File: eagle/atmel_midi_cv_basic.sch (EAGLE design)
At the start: 46 parts, among them IC1 TL074P, Q2 2N3904, U1 ATMEGA328P_PDIP

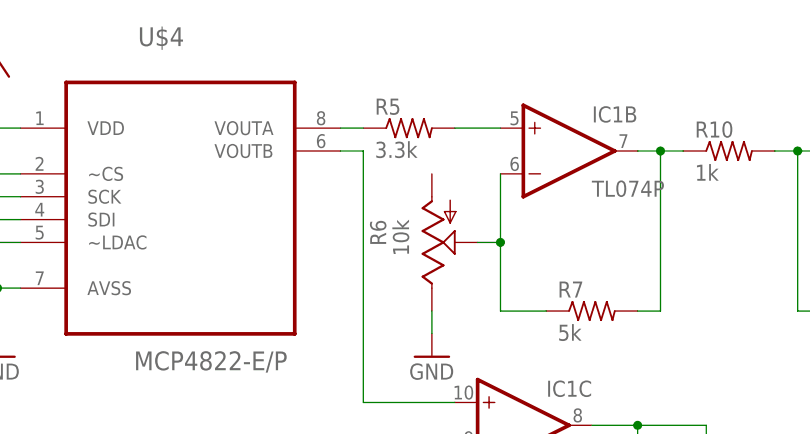
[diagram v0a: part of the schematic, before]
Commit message: playing scale to indicate midi channel by number of notes
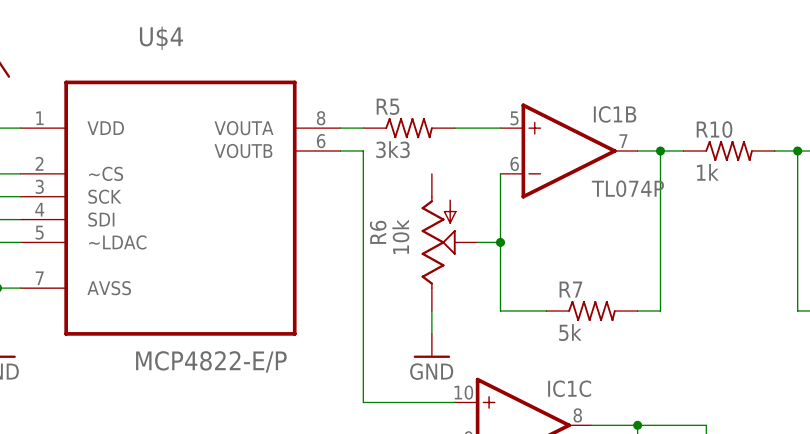
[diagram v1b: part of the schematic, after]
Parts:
- R5: value 3.3k -> 3k3
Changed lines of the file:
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@@
 <?xml version="1.0" encoding="utf-8"?>
 <!DOCTYPE eagle SYSTEM "eagle.dtd">
-<eagle version="7.2.0">
+<eagle version="7.1.0">
 <drawing>
 <settings>
@@
 <part name="GND1" library="supply1" deviceset="GND" device=""/>
 <part name="GND2" library="supply1" deviceset="GND" device=""/>
-<part name="R5" library="rcl" deviceset="R-US_" device="0207/10" value="3.3k"/>
+<part name="R5" library="rcl" deviceset="R-US_" device="0207/10" value="3k3"/>
 <part name="R6" library="pot" deviceset="TRIM_US-" device="B64W" value="10k"/>
 <part name="GND4" library="supply1" deviceset="GND" device=""/>

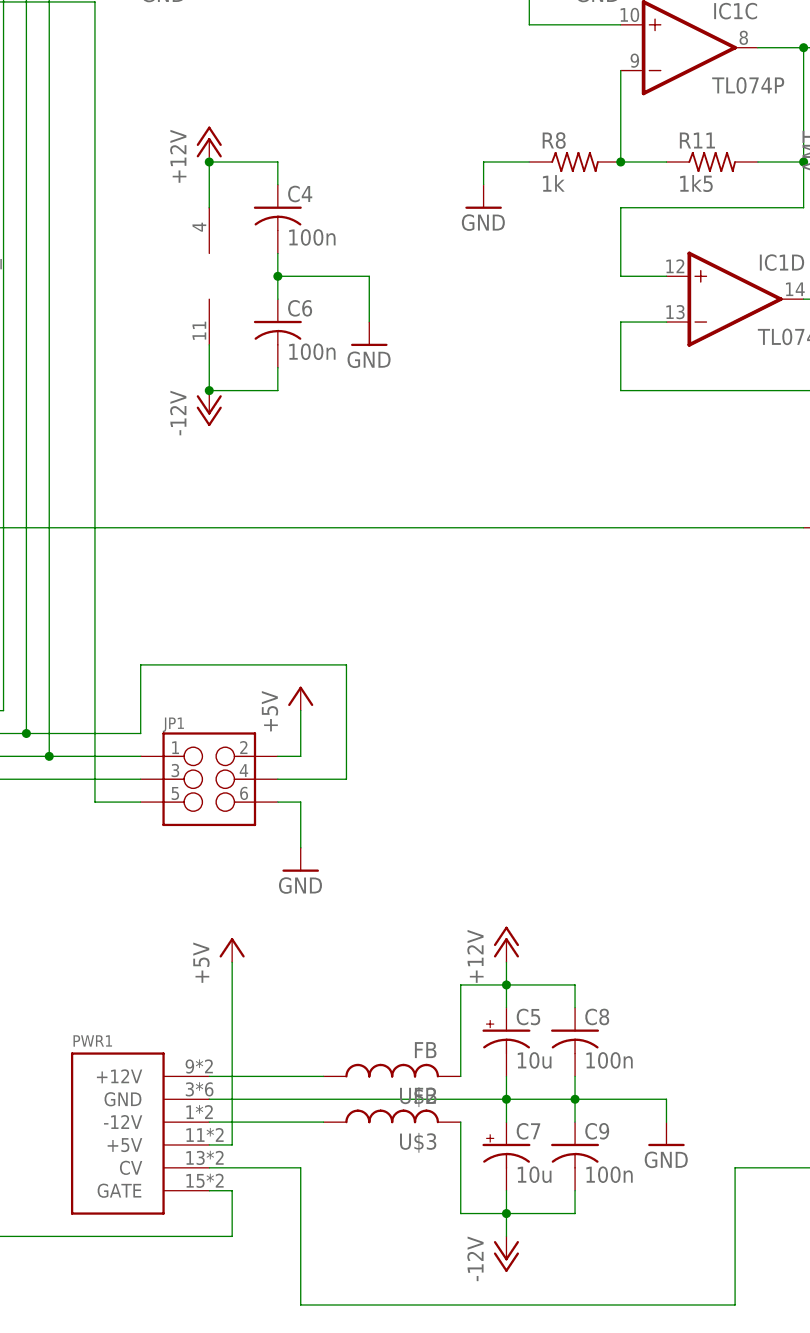
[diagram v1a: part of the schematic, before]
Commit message: no neg supply
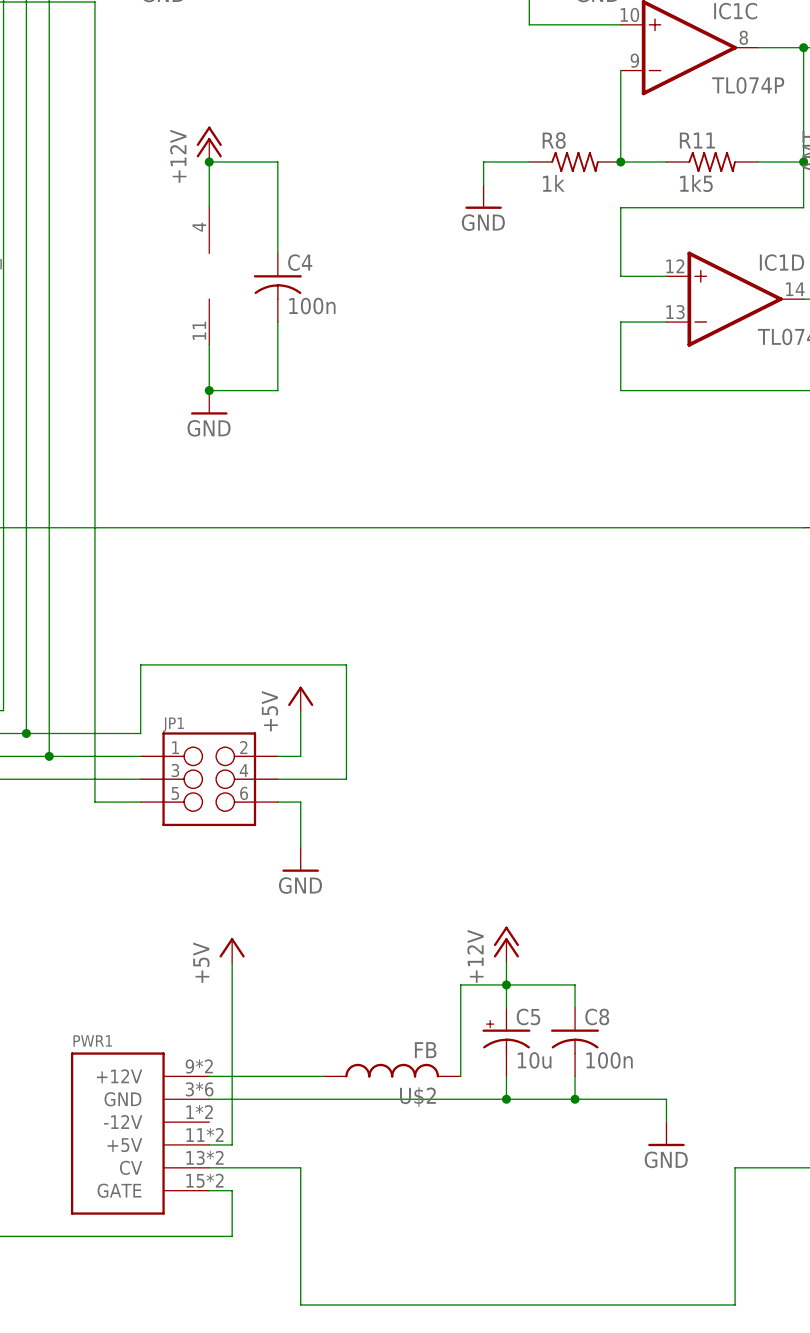
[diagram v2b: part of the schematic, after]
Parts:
- removed C6, C9: 100n, rcl:C-US050-024X044
- removed C7: 10u, rcl:CPOL-USB45181A
- removed U$3: FB, adafruit:FB
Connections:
- removed net -12V: C6.2, C7.-, C9.2, IC1P.V-, U$3.2
- removed net N$18: PWR1.-12V, U$3.1
- net GND: now also IC1P.V-; no longer C6.1, C7.+, C9.1
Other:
- moved on the sheet: C4
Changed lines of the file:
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@@
 <part name="PWR1" library="eurorack" deviceset="POWER" device=""/>
 <part name="U$2" library="adafruit" deviceset="FB" device=""/>
-<part name="U$3" library="adafruit" deviceset="FB" device=""/>
 <part name="C5" library="rcl" deviceset="CPOL-US" device="B45181A" value="10u"/>
-<part name="C7" library="rcl" deviceset="CPOL-US" device="B45181A" value="10u"/>
 <part name="P+5" library="supply1" deviceset="+12V" device=""/>
-<part name="P-2" library="supply1" deviceset="-12V" device=""/>
 <part name="GND6" library="supply1" deviceset="GND" device=""/>
 <part name="C8" library="rcl" deviceset="C-US" device="050-024X044" value="100n"/>
-<part name="C9" library="rcl" deviceset="C-US" device="050-024X044" value="100n"/>
 <part name="PITCH" library="erthenvar" deviceset="AUDIO-JACK" device=""/>
 <part name="VEL" library="erthenvar" deviceset="AUDIO-JACK" device=""/>
@@
 <part name="Q2" library="transistor-npn" deviceset="2N3904" device=""/>
 <part name="C4" library="rcl" deviceset="C-US" device="050-024X044" value="100n"/>
-<part name="C6" library="rcl" deviceset="C-US" device="050-024X044" value="100n"/>
 <part name="GND8" library="supply1" deviceset="GND" device=""/>
 <part name="P+4" library="supply1" deviceset="+12V" device=""/>
-<part name="P-1" library="supply1" deviceset="-12V" device=""/>
 <part name="P+7" library="supply1" deviceset="+5V" device=""/>
 <part name="R4" library="rcl" deviceset="R-US_" device="0207/10" value="3k3"/>
@@
 <instance part="PWR1" gate="G$1" x="76.2" y="-22.86"/>
 <instance part="U$2" gate="G$1" x="106.68" y="-17.78" rot="R90"/>
-<instance part="U$3" gate="G$1" x="106.68" y="-22.86" rot="R90"/>
 <instance part="C5" gate="G$1" x="119.38" y="-12.7"/>
-<instance part="C7" gate="G$1" x="119.38" y="-25.4"/>
 <instance part="P+5" gate="1" x="119.38" y="-2.54"/>
-<instance part="P-2" gate="1" x="119.38" y="-38.1"/>
 <instance part="GND6" gate="1" x="137.16" y="-25.4"/>
 <instance part="C8" gate="G$1" x="127" y="-12.7"/>
-<instance part="C9" gate="G$1" x="127" y="-25.4"/>
 <instance part="PITCH" gate="G$1" x="182.88" y="121.92" rot="R180"/>
 <instance part="VEL" gate="G$1" x="175.26" y="81.28" rot="R180"/>
@@
 <instance part="Q2" gate="G1" x="175.26" y="43.18"/>
 <instance part="IC1" gate="D" x="144.78" y="68.58"/>
-<instance part="C4" gate="G$1" x="93.98" y="78.74"/>
-<instance part="C6" gate="G$1" x="93.98" y="66.04"/>
-<instance part="GND8" gate="1" x="104.14" y="63.5"/>
+<instance part="C4" gate="G$1" x="93.98" y="71.12"/>
+<instance part="GND8" gate="1" x="86.36" y="55.88"/>
 <instance part="P+4" gate="1" x="86.36" y="86.36"/>
-<instance part="P-1" gate="1" x="86.36" y="55.88"/>
 <instance part="P+7" gate="1" x="88.9" y="-2.54"/>
 <instance part="R4" gate="G$1" x="157.48" y="43.18" rot="R180"/>
@@
 <wire x1="119.38" y1="-17.78" x2="119.38" y2="-20.32" width="0.1524" layer="91"/>
 <junction x="119.38" y="-20.32"/>
-<pinref part="C7" gate="G$1" pin="+"/>
-<wire x1="119.38" y1="-22.86" x2="119.38" y2="-20.32" width="0.1524" layer="91"/>
 <pinref part="C8" gate="G$1" pin="2"/>
 <wire x1="127" y1="-17.78" x2="127" y2="-20.32" width="0.1524" layer="91"/>
 <junction x="127" y="-20.32"/>
-<pinref part="C9" gate="G$1" pin="1"/>
-<wire x1="127" y1="-22.86" x2="127" y2="-20.32" width="0.1524" layer="91"/>
 </segment>
 <segment>
@@
 <segment>
 <pinref part="GND8" gate="1" pin="GND"/>
-<wire x1="104.14" y1="66.04" x2="104.14" y2="71.12" width="0.1524" layer="91"/>
-<pinref part="C6" gate="G$1" pin="1"/>
+<wire x1="86.36" y1="58.42" x2="93.98" y2="58.42" width="0.1524" layer="91"/>
 <pinref part="C4" gate="G$1" pin="2"/>
-<wire x1="93.98" y1="73.66" x2="93.98" y2="71.12" width="0.1524" layer="91"/>
-<wire x1="93.98" y1="71.12" x2="93.98" y2="68.58" width="0.1524" layer="91"/>
-<wire x1="104.14" y1="71.12" x2="93.98" y2="71.12" width="0.1524" layer="91"/>
-<junction x="93.98" y="71.12"/>
+<wire x1="93.98" y1="58.42" x2="93.98" y2="66.04" width="0.1524" layer="91"/>
+<pinref part="IC1" gate="P" pin="V-"/>
+<wire x1="86.36" y1="63.5" x2="86.36" y2="58.42" width="0.1524" layer="91"/>
+<junction x="86.36" y="58.42"/>
 </segment>
 <segment>
@@
 <segment>
 <pinref part="C4" gate="G$1" pin="1"/>
-<wire x1="93.98" y1="81.28" x2="93.98" y2="83.82" width="0.1524" layer="91"/>
+<wire x1="93.98" y1="73.66" x2="93.98" y2="83.82" width="0.1524" layer="91"/>
 <wire x1="93.98" y1="83.82" x2="86.36" y2="83.82" width="0.1524" layer="91"/>
 <wire x1="86.36" y1="83.82" x2="86.36" y2="78.74" width="0.1524" layer="91"/>
@@
 <junction x="86.36" y="83.82"/>
 <pinref part="IC1" gate="P" pin="V+"/>
-</segment>
-</net>
-<net name="-12V" class="0">
-<segment>
-<pinref part="C7" gate="G$1" pin="-"/>
-<pinref part="P-2" gate="1" pin="-12V"/>
-<wire x1="119.38" y1="-35.56" x2="119.38" y2="-33.02" width="0.1524" layer="91"/>
-<pinref part="U$3" gate="G$1" pin="2"/>
-<wire x1="119.38" y1="-33.02" x2="119.38" y2="-30.48" width="0.1524" layer="91"/>
-<wire x1="114.3" y1="-22.86" x2="114.3" y2="-33.02" width="0.1524" layer="91"/>
-<wire x1="114.3" y1="-33.02" x2="119.38" y2="-33.02" width="0.1524" layer="91"/>
-<junction x="119.38" y="-33.02"/>
-<pinref part="C9" gate="G$1" pin="2"/>
-<wire x1="127" y1="-30.48" x2="127" y2="-33.02" width="0.1524" layer="91"/>
-<wire x1="127" y1="-33.02" x2="119.38" y2="-33.02" width="0.1524" layer="91"/>
-</segment>
-<segment>
-<wire x1="86.36" y1="63.5" x2="86.36" y2="58.42" width="0.1524" layer="91"/>
-<pinref part="C6" gate="G$1" pin="2"/>
-<wire x1="86.36" y1="58.42" x2="93.98" y2="58.42" width="0.1524" layer="91"/>
-<wire x1="93.98" y1="58.42" x2="93.98" y2="60.96" width="0.1524" layer="91"/>
-<pinref part="P-1" gate="1" pin="-12V"/>
-<junction x="86.36" y="58.42"/>
-<pinref part="IC1" gate="P" pin="V-"/>
 </segment>
 </net>
@@
 </segment>
 </net>
-<net name="N$18" class="0">
-<segment>
-<pinref part="PWR1" gate="G$1" pin="-12V"/>
-<pinref part="U$3" gate="G$1" pin="1"/>
-<wire x1="86.36" y1="-22.86" x2="99.06" y2="-22.86" width="0.1524" layer="91"/>
-</segment>
-</net>

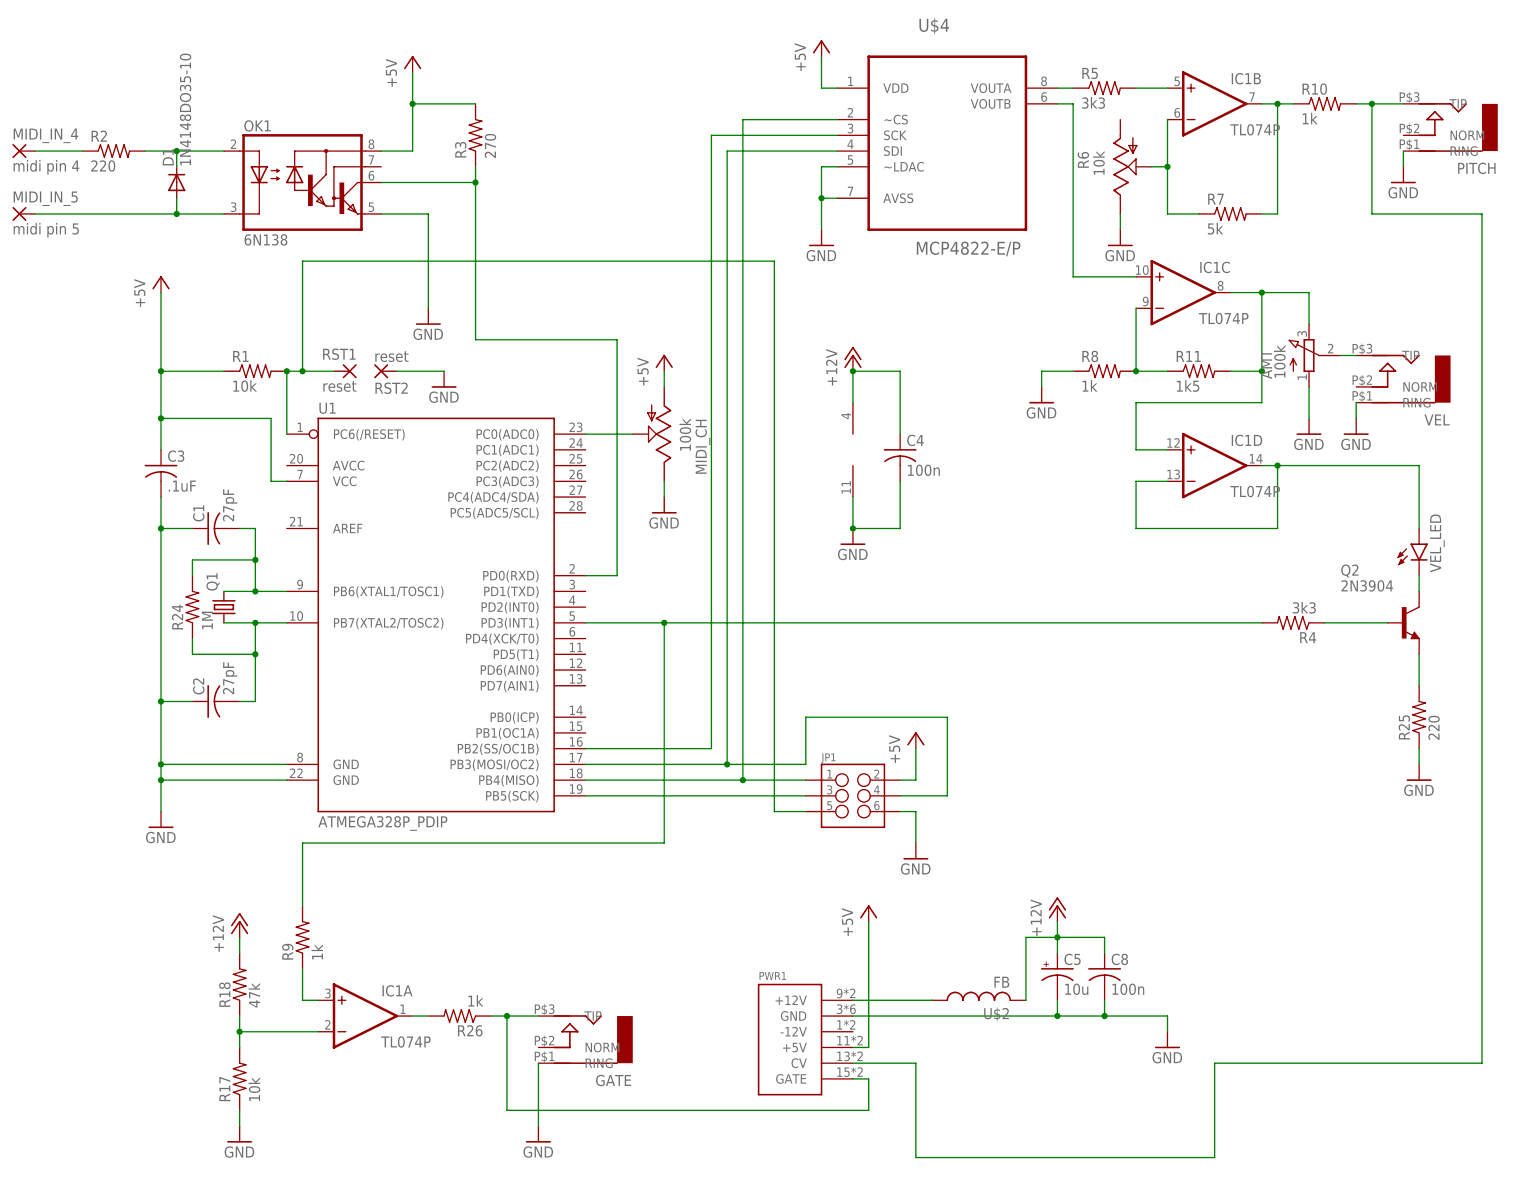
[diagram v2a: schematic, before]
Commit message: swapping atmega pin 16 and 17 for layout convenience
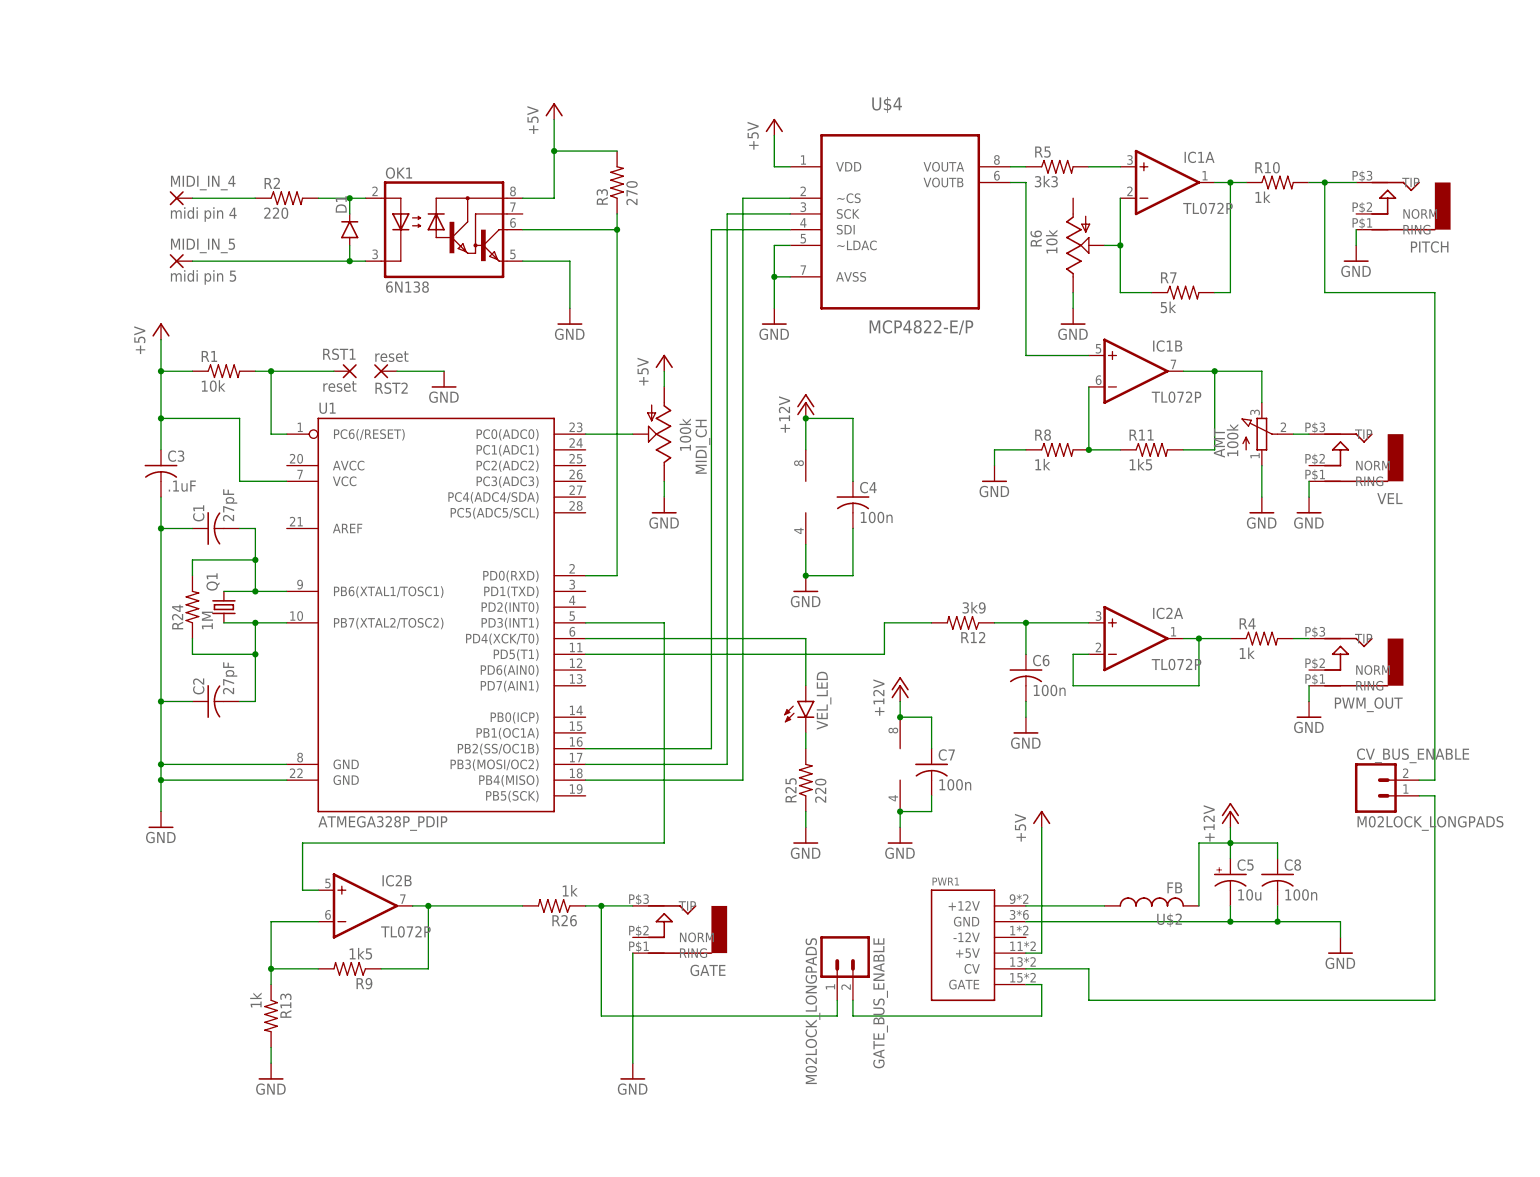
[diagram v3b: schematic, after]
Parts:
- removed JP1: (no value), SparkFun-Connectors:M03X2NO_SILK
- removed Q2: 2N3904, transistor-npn:2N3904
- removed R17: 10k, rcl:R-US_0207/10
- removed R18: 47k, rcl:R-US_0207/10
- added C6, C7: 100n, rcl:C-US050-024X044
- added CV_BUS_ENABLE, GATE_BUS_ENABLE: M02LOCK_LONGPADS, SparkFun-Connectors:M02LOCK_LONGPADS
- added IC2: TL072P, linear:TL072P
- added PWM_OUT: AUDIO-JACK, erthenvar:AUDIO-JACK
- added R12: 3k9, rcl:R-US_0207/10
- added R13: 1k, rcl:R-US_0207/10
- D1: value 1N4148DO35-10 -> (none); device diode:1N4148DO35-10 -> SparkFun-DiscreteSemi:DIODE1N4148
- IC1: value TL074P -> TL072P; device linear:TL074P -> linear:TL072P
- R4: value 3k3 -> 1k
- R9: value 1k -> 1k5
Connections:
- new net N$18: R25.2, VEL_LED.C
- new net N$28: C6.1, IC2A.+IN, R12.1
- net +12V: now also C7.1, IC2P.V+; no longer R18.2
- net +5V: no longer JP1.2
- net GND: now also C6.2, C7.2, IC2P.V-, PWM_OUT.RING, R13.2; no longer JP1.6, R17.1
- net N$1: now also GATE_BUS_ENABLE.2, PWR1.GATE; no longer IC1A.+IN, R9.1
- net N$10: now also IC2B.-IN, R13.1, R9.2; no longer JP1.3, U1.PB5(SCK)
- net N$12: now also IC1A.-IN; no longer IC1B.-IN
- net N$13: now also IC1B.-IN; no longer IC1C.-IN
- net N$14: now also IC1B.+IN; no longer IC1C.+IN
- net N$15: now also CV_BUS_ENABLE.1, PWR1.CV; no longer IC1A.-IN, R17.2, R18.1
- net N$16: now also IC2B.OUT, R9.1; no longer IC1A.OUT
- net N$17: now also IC1B.OUT; no longer IC1C.OUT, IC1D.+IN
- net N$20: now also U1.PD4(XCK/T0), VEL_LED.A; no longer Q2.C, VEL_LED.C
- net N$21: now also R12.2, U1.PD5(T1); no longer IC1D.-IN, IC1D.OUT, VEL_LED.A
- net N$22: now also IC2B.+IN; no longer R4.2, R9.2
- net N$23: now also IC2A.-IN, IC2A.OUT; no longer Q2.B
- net N$24: now also PWM_OUT.TIP, R4.2; no longer Q2.E, R25.2
- net N$25: now also U1.PB3(MOSI/OC2); no longer U1.PB2(SS/OC1B)
- net N$26: now also U1.PB2(SS/OC1B); no longer JP1.4, U1.PB3(MOSI/OC2)
- net N$27: now also IC1A.OUT; no longer IC1B.OUT
- net N$31: now also GATE_BUS_ENABLE.1; no longer PWR1.GATE
- net N$43: no longer JP1.5
- net N$45: no longer JP1.1
- net N$6: now also IC1A.+IN; no longer IC1B.+IN
- net N$9: now also CV_BUS_ENABLE.2; no longer PWR1.CV
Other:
- moved on the sheet: AMT, C4, C5, C8, GATE, IC1A, IC1B, MIDI_IN_4, MIDI_IN_5, OK1, PITCH, PWR1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
